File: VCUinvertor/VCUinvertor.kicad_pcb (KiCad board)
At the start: 2 copper layers, 154 x 113.8 mm, 71 parts, among them J1 NXP1, J2 Conn_02x10_Odd_Even, J3 NXP2, J4 Conn_02x10_Odd_Even, J5 Conn_02x10_Odd_Even, J6 Conn_02x10_Odd_Even, J7 PowerSupply, Q1 BSS138, Q10 BSS138, Q2 BSS138, Q3 BSS138, Q4 BSS138, Q5 BSS138, Q6 BSS138, Q7 BSS138, Q8 BSS138, Q9 BSS138, U1 TJA1448ATK, U2 REF3433T, U2 TJA1443ATK, U3 TLV76150DCY

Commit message: Footprint assignment
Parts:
- removed the U2 at (148.1, 100.9)
- added C1: 0.1uF, Capacitor_SMD:C_0805_2012Metric_Pad1.18x1.45mm_HandSolder, F.Cu at (204.1, 92.4)
- added C10: 0.1uF, Capacitor_SMD:C_0805_2012Metric_Pad1.18x1.45mm_HandSolder, F.Cu at (208.9, 101.5)
- added C11: 10uF, Capacitor_SMD:C_0805_2012Metric_Pad1.18x1.45mm_HandSolder, F.Cu at (208.9, 104.5)
- added C2: 0.1uF, Capacitor_SMD:C_0805_2012Metric_Pad1.18x1.45mm_HandSolder, F.Cu at (204.1, 95.4)
- added C3: 0.1uF, Capacitor_SMD:C_0805_2012Metric_Pad1.18x1.45mm_HandSolder, F.Cu at (204.1, 98.5)
- added C4: 2.2uF, Capacitor_SMD:C_0805_2012Metric_Pad1.18x1.45mm_HandSolder, F.Cu at (204.1, 101.5)
- added C5: 0.1uF, Capacitor_SMD:C_0805_2012Metric_Pad1.18x1.45mm_HandSolder, F.Cu at (204.1, 104.5)
- added C6: 0.1uF, Capacitor_SMD:C_0805_2012Metric_Pad1.18x1.45mm_HandSolder, F.Cu at (204.1, 107.5)
- added C7: 4.7uF, Capacitor_SMD:C_0805_2012Metric_Pad1.18x1.45mm_HandSolder, F.Cu at (208.9, 92.4)
- added C8: 4.7uF, Capacitor_SMD:C_0805_2012Metric_Pad1.18x1.45mm_HandSolder, F.Cu at (208.9, 95.4)
- added C9: 10uF, Capacitor_SMD:C_0805_2012Metric_Pad1.18x1.45mm_HandSolder, F.Cu at (208.9, 98.5)
- added DAC1: LTC2645HMS-L12_PBF, Package_SO:MSOP-16-1EP_3x4.039mm_P0.5mm_EP1.651x2.845mm, F.Cu at (164.1, 100.2)
- added Q1: BSS138, Package_TO_SOT_SMD:SOT-23, F.Cu at (194.3, 93.2)
- added Q10: BSS138, Package_TO_SOT_SMD:SOT-23, F.Cu at (199.2, 111.0)
- added Q2: BSS138, Package_TO_SOT_SMD:SOT-23, F.Cu at (194.3, 97.6)
- added Q3: BSS138, Package_TO_SOT_SMD:SOT-23, F.Cu at (194.3, 102.0)
- added Q4: BSS138, Package_TO_SOT_SMD:SOT-23, F.Cu at (194.3, 106.5)
- added Q5: BSS138, Package_TO_SOT_SMD:SOT-23, F.Cu at (194.3, 111.0)
- added Q6: BSS138, Package_TO_SOT_SMD:SOT-23, F.Cu at (199.2, 93.2)
- added Q7: BSS138, Package_TO_SOT_SMD:SOT-23, F.Cu at (199.2, 97.6)
- added Q8: BSS138, Package_TO_SOT_SMD:SOT-23, F.Cu at (199.2, 102.0)
- added Q9: BSS138, Package_TO_SOT_SMD:SOT-23, F.Cu at (199.2, 106.5)
- added R1: 60R4, Resistor_SMD:R_0805_2012Metric, F.Cu at (176.4, 92.4)
- added R10: 5k, Resistor_SMD:R_0805_2012Metric, F.Cu at (180.8, 95.3)
- added R11: 5k, Resistor_SMD:R_0805_2012Metric, F.Cu at (180.8, 98.3)
- added R12: 5k, Resistor_SMD:R_0805_2012Metric, F.Cu at (180.8, 101.2)
- added R13: 5k, Resistor_SMD:R_0805_2012Metric, F.Cu at (180.8, 104.2)
- added R14: 5k, Resistor_SMD:R_0805_2012Metric, F.Cu at (180.8, 107.2)
- added R15: 10k, Resistor_SMD:R_0805_2012Metric, F.Cu at (180.8, 110.1)
- added R16: 5k, Resistor_SMD:R_0805_2012Metric, F.Cu at (180.8, 113.0)
- added R17: 10k, Resistor_SMD:R_0805_2012Metric, F.Cu at (185.3, 92.4)
- added R18: 5k, Resistor_SMD:R_0805_2012Metric, F.Cu at (185.3, 95.3)
- added R19: 10k, Resistor_SMD:R_0805_2012Metric, F.Cu at (185.3, 98.3)
- added R2: 60R4, Resistor_SMD:R_0805_2012Metric, F.Cu at (176.4, 95.3)
- added R20: 5k, Resistor_SMD:R_0805_2012Metric, F.Cu at (185.3, 101.2)
- added R21: 10k, Resistor_SMD:R_0805_2012Metric, F.Cu at (185.3, 104.2)
- added R22: 5k, Resistor_SMD:R_0805_2012Metric, F.Cu at (185.3, 107.2)
- added R23: 10k, Resistor_SMD:R_0805_2012Metric, F.Cu at (185.3, 110.1)
- added R24: 5k, Resistor_SMD:R_0805_2012Metric, F.Cu at (185.3, 113.0)
- added R25: 5.1k, Resistor_SMD:R_0805_2012Metric, F.Cu at (189.7, 92.4)
- added R26: 10k, Resistor_SMD:R_0805_2012Metric, F.Cu at (189.7, 95.3)
- added R27: 5.1k, Resistor_SMD:R_0805_2012Metric, F.Cu at (189.7, 98.3)
- added R28: 10k, Resistor_SMD:R_0805_2012Metric, F.Cu at (189.7, 101.2)
- added R3: 60R4, Resistor_SMD:R_0805_2012Metric, F.Cu at (176.4, 98.3)
- added R4: 60R4, Resistor_SMD:R_0805_2012Metric, F.Cu at (176.4, 101.2)
- added R5: 10k, Resistor_SMD:R_0805_2012Metric, F.Cu at (176.4, 104.2)
- added R6: 10k, Resistor_SMD:R_0805_2012Metric, F.Cu at (176.4, 107.2)
- added R7: 10k, Resistor_SMD:R_0805_2012Metric, F.Cu at (176.4, 110.1)
- added R8: 10k, Resistor_SMD:R_0805_2012Metric, F.Cu at (176.4, 113.0)
- added R9: 10k, Resistor_SMD:R_0805_2012Metric, F.Cu at (180.8, 92.4)
- moved JO19 121.0 mm to (249.5, 130.5), turned to 90 degrees
- moved JO11 118.7 mm to (244.8, 130.5), turned to 90 degrees
- moved JO9 116.6 mm to (240.2, 130.5), turned to 90 degrees
- moved JO5 114.9 mm to (235.5, 130.5), turned to 90 degrees
- moved JO3 113.6 mm to (230.9, 130.5), turned to 90 degrees
- moved JO1 76.6 mm to (231.8, 93.6)
- moved JO13 76.6 mm to (246.3, 93.6)
- moved JO14 76.6 mm to (246.3, 98.2)
- moved JO15 76.6 mm to (246.3, 102.9)
- moved JO16 76.6 mm to (246.3, 107.5)
- moved JO17 76.6 mm to (251.2, 93.6)
- moved JO18 76.6 mm to (251.2, 98.2)
- moved JO19 76.6 mm to (251.2, 102.9)
- moved JO2 76.6 mm to (231.8, 98.2)
- moved JO20 76.6 mm to (251.2, 107.5)
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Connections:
- J3 pad 10: unconnected-(J3-Pin_10-Pad10) -> /TX1
- J3 pad 12: unconnected-(J3-Pin_12-Pad12) -> /RX1
- J3 pad 18: unconnected-(J3-Pin_18-Pad18) -> NXP_TPSOUT01
- J3 pad 2: unconnected-(J3-Pin_2-Pad2) -> /Pxx
- J3 pad 20: unconnected-(J3-Pin_20-Pad20) -> NXP_TPSOUT02
- J3 pad 4: unconnected-(J3-Pin_4-Pad4) -> /Pyy
- J3 pad 6: unconnected-(J3-Pin_6-Pad6) -> /TX0
- J3 pad 8: unconnected-(J3-Pin_8-Pad8) -> /RX0
- J4 pad 10: unconnected-(J4-Pin_10-Pad10) -> /NXP_ACC01
- J4 pad 12: unconnected-(J4-Pin_12-Pad12) -> /NXP_ECO01
- J4 pad 14: unconnected-(J4-Pin_14-Pad14) -> /NXP_BRK01
- J4 pad 16: unconnected-(J4-Pin_16-Pad16) -> /NXP_FWD01
- J4 pad 18: unconnected-(J4-Pin_18-Pad18) -> /NXP_REV01
- J4 pad 2: unconnected-(J4-Pin_2-Pad2) -> /PWM_NXP4
- J4 pad 20: unconnected-(J4-Pin_20-Pad20) -> BACKLIGHT_ON
- J4 pad 4: unconnected-(J4-Pin_4-Pad4) -> /PWM_NXP3
- J4 pad 6: unconnected-(J4-Pin_6-Pad6) -> /PWM_NXP2
- J4 pad 8: unconnected-(J4-Pin_8-Pad8) -> /PWM_NXP1
- J6 pad 10: unconnected-(J6-Pin_10-Pad10) -> /NXP_REV02
- J6 pad 2: unconnected-(J6-Pin_2-Pad2) -> /NXP_ACC02
- J6 pad 4: unconnected-(J6-Pin_4-Pad4) -> /NXP_ECO02
- J6 pad 6: unconnected-(J6-Pin_6-Pad6) -> /NXP_BRK02
- J6 pad 8: unconnected-(J6-Pin_8-Pad8) -> /NXP_FWD02
- JO11 pad 1: Net-(JO11-Pin_1) -> /ECO1
- JO19 pad 1: Net-(JO19-Pin_1) -> /ACC1
- JO22 pad 1: Net-(JO22-Pin_1) -> /REV2
- JO23 pad 1: Net-(JO23-Pin_1) -> /FWD2
- JO25 pad 1: Net-(JO25-Pin_1) -> /H_Brk2
- JO29 pad 1: Net-(JO29-Pin_1) -> /ECO2
- JO3 pad 1: Net-(JO3-Pin_1) -> /REV1
- JO31 pad 1: Net-(JO31-Pin_1) -> /ACC2
- JO5 pad 1: Net-(JO5-Pin_1) -> /FWD1
- JO9 pad 1: Net-(JO9-Pin_1) -> /H_Brk1
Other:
- board size 154 x 113.8 mm -> 210.5 x 113.8 mm

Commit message: Layout_Global arrangement
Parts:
- removed D2: 1N4148WT, Diode_SMD:D_SOD-523
- removed the JO11 at (241.4, 102.9)
- removed JO16, JO17, JO18, JO20, JO36, JO37, JO38, JO39, JO40: -, Connector_Wire:SolderWire-0.75sqmm_1x01_D1.25mm_OD2.3mm
- removed the JO19 at (251.2, 102.9)
- removed JO2: -REV (Orange), Connector_Wire:SolderWire-0.75sqmm_1x01_D1.25mm_OD2.3mm
- removed the JO3 at (231.8, 102.9)
- removed the JO5 at (236.6, 93.6)
- removed the JO9 at (241.4, 93.6)
- removed the Q1 at (142.5, 65.5)
- removed the Q1 at (194.3, 93.2)
- removed the Q10 at (199.2, 111.0)
- removed the Q10 at (147.4, 83.3)
- removed the Q2 at (142.5, 70.0)
- removed the Q2 at (194.3, 97.6)
- removed the Q3 at (142.5, 74.4)
- removed the Q3 at (194.3, 102.0)
- removed the Q4 at (142.5, 78.9)
- removed the Q4 at (194.3, 106.5)
- removed the Q5 at (142.5, 83.3)
- removed the Q5 at (194.3, 111.0)
- removed the Q6 at (199.2, 93.2)
- removed the Q6 at (147.4, 65.5)
- removed the Q7 at (147.4, 70.0)
- removed the Q7 at (199.2, 97.6)
- removed the Q8 at (147.4, 74.4)
- removed the Q8 at (199.2, 102.0)
- removed the Q9 at (199.2, 106.5)
- removed the Q9 at (147.4, 78.9)
- added J8: CAN_NXP, Connector_PinHeader_2.54mm:PinHeader_1x04_P2.54mm_Vertical, B.Cu at (85.3, 48.0)
- added J9: BACKLIGHT, Connector_JST:JST_PH_B3B-PH-K_1x03_P2.00mm_Vertical, B.Cu at (110.0, 40.6)
- added Q1: BSS138, Package_TO_SOT_SMD:SOT-23, B.Cu at (126.3, 131.0)
- added Q10: BSS138, Package_TO_SOT_SMD:SOT-23, B.Cu at (126.0, 57.6)
- added Q2: BSS138, Package_TO_SOT_SMD:SOT-23, B.Cu at (126.3, 125.7)
- added Q3: BSS138, Package_TO_SOT_SMD:SOT-23, B.Cu at (126.3, 120.2)
- added Q4: BSS138, Package_TO_SOT_SMD:SOT-23, B.Cu at (126.8, 114.9)
- added Q5: BSS138, Package_TO_SOT_SMD:SOT-23, B.Cu at (127.1, 109.5)
- added Q6: BSS138, Package_TO_SOT_SMD:SOT-23, B.Cu at (125.4, 81.1)
- added Q7: BSS138, Package_TO_SOT_SMD:SOT-23, B.Cu at (125.5, 74.5)
- added Q8: BSS138, Package_TO_SOT_SMD:SOT-23, B.Cu at (125.8, 69.1)
- added Q9: BSS138, Package_TO_SOT_SMD:SOT-23, B.Cu at (125.8, 63.5)
- C3, C4, CA1, J7, JU1, JU2, R10, R11, R12, R13, R14, R15, R16, R17, R18, R19, R20, R21, R22, R23, R24, R5, R6, R7, R8, R9, U3: moved to B.Cu
- J1: value NXP1 -> NXP12
- J2: value Conn_02x10_Odd_Even -> NXP11
- J3: value NXP2 -> NXP15
- J4: value Conn_02x10_Odd_Even -> NXP14
- J5: value Conn_02x10_Odd_Even -> NXP10
- J6: value Conn_02x10_Odd_Even -> NXP13
- moved JU2 148.8 mm to (82.7, 146.9), turned to 180 degrees
- moved C10 134.5 mm to (75.2, 115.6), turned to 90 degrees
- moved C9 132.8 mm to (77.3, 115.6), turned to 90 degrees
- moved JU1 130.9 mm to (95.2, 146.8), turned to 180 degrees
- moved C4 123.1 mm to (88.0, 60.5), turned to 90 degrees
- moved C8 120.8 mm to (91.1, 121.8), turned to 180 degrees
- moved C7 120.4 mm to (91.2, 117.7), turned to 180 degrees
- moved C3 114.4 mm to (97.7, 56.4), turned to -90 degrees
- moved C11 112.6 mm to (97.3, 89.8), turned to -90 degrees
- moved JO14 110.9 mm to (141.4, 134.1), turned to 90 degrees
- moved C1 109.5 mm to (94.8, 98.2), turned to 90 degrees
- moved JO19 109.1 mm to (141.2, 116.8)
- moved JO34 107.7 mm to (141.4, 84.4)
- moved JO35 105.3 mm to (141.4, 67.6)
- moved C6 105.3 mm to (98.8, 108.5)
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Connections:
- net Net-(DAC1-VOUTA) renamed /Brk_AN1
- net Net-(DAC1-VOUTC) renamed /Brk_AN2
- J6 pad 13: unconnected-(J6-Pin_13-Pad13) -> GND
- J6 pad 15: unconnected-(J6-Pin_15-Pad15) -> +12V
- JO26 pad 1: GND -> unconnected-(JO26-Pin_1-Pad1)
- JO6 pad 1: GND -> unconnected-(JO6-Pin_1-Pad1)
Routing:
- net GND: track 0.00 -> 24.6 mm
- net +5V: track 0.00 -> 17.1 mm
- net /Brk_AN2: track 0.00 -> 14.0 mm, vias 0 -> 1
- net +3.3V: track 0.00 -> 13.1 mm
- net /PWM_NXP3: track 0.00 -> 11.5 mm, vias 0 -> 1
- net /PWM_NXP4: track 0.00 -> 11.0 mm, vias 0 -> 1
- net /PWM_NXP1: track 0.00 -> 10.7 mm, vias 0 -> 1
- net /PWM_NXP2: track 0.00 -> 9.41 mm, vias 0 -> 1
- net /Brk_AN1: track 0.00 -> 7.60 mm, vias 0 -> 1
- net /H_Brk2: track 0.00 -> 6.94 mm
- net /REV2: track 0.00 -> 6.72 mm
- net /ECO2: track 0.00 -> 6.64 mm
- net unconnected-(JO26-Pin_1-Pad1): track 0.00 -> 6.44 mm
- net /CANL02: track 0.00 -> 6.00 mm
- net /CANH02: track 0.00 -> 5.40 mm
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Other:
- board size 210.5 x 113.8 mm -> 97.3 x 113.8 mm

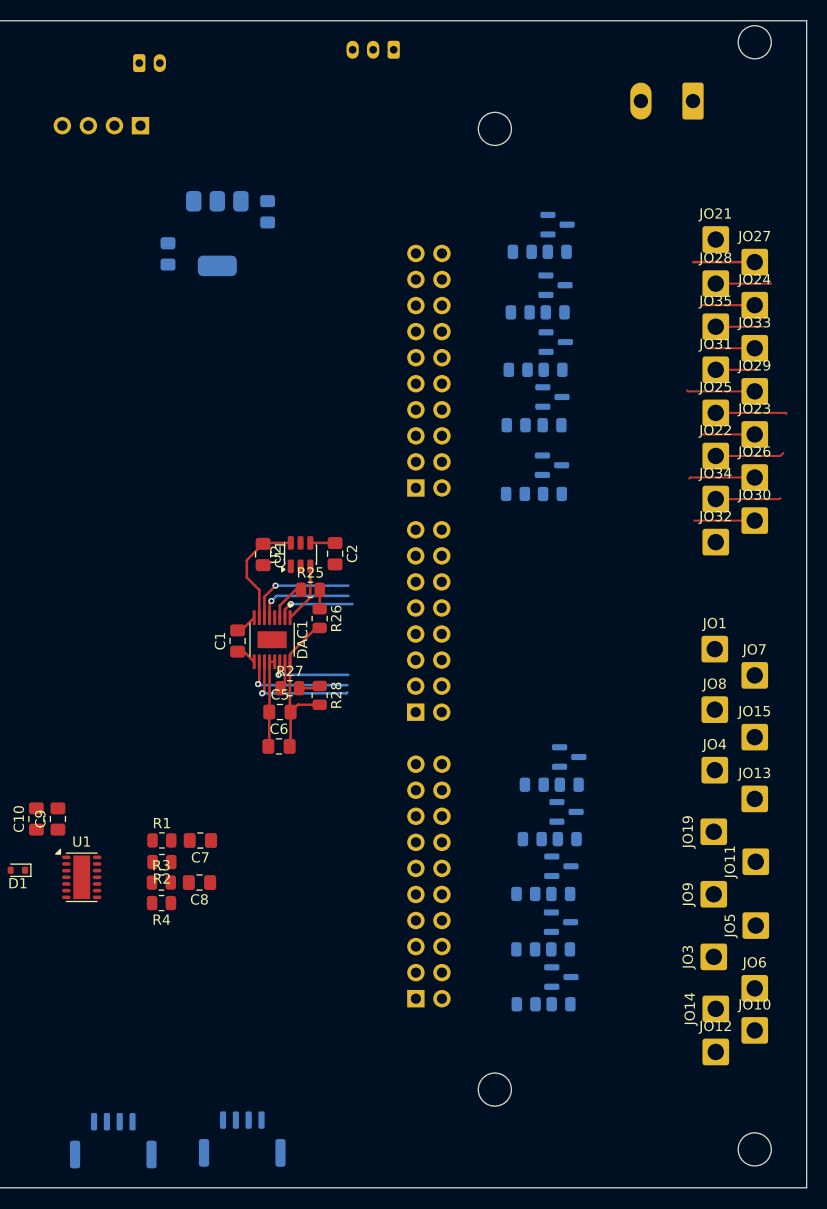
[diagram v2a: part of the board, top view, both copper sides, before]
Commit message: DAQ footprint correction
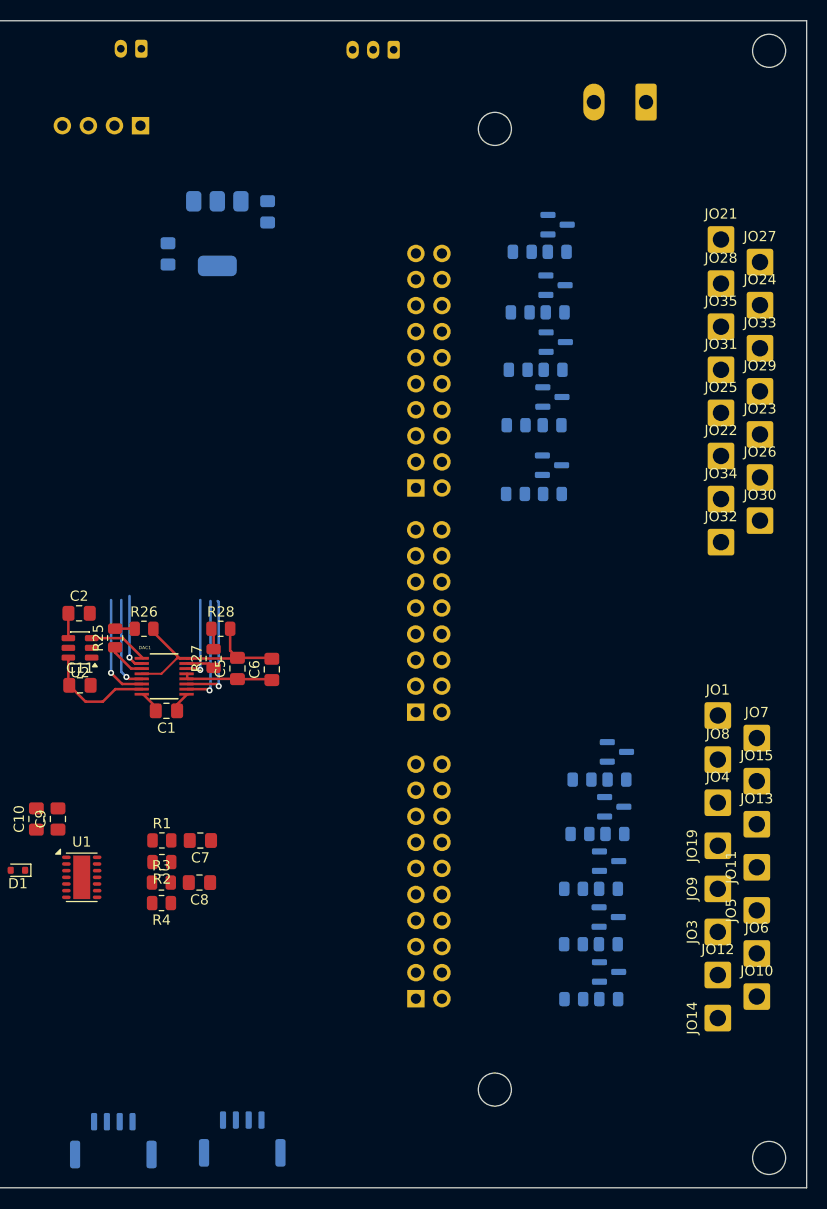
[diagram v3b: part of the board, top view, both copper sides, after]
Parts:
- DAC1: footprint Package_SO:MSOP-16-1EP_3x4.039mm_P0.5mm_EP1.651x2.845mm -> LTC2645HMS-L12_PBF:MSOP-16_MS
- moved C2 25.6 mm to (79.3, 95.5), turned to 0 degrees
- moved U2 23.3 mm to (79.4, 98.9), turned to 180 degrees
- moved C11 21.9 mm to (79.4, 102.6), turned to 0 degrees
- moved R25 19.6 mm to (82.8, 97.9), turned to 90 degrees
- moved R26 17.2 mm to (85.7, 97.0), turned to 0 degrees
- moved R28 11.6 mm to (93.1, 97.0), turned to 0 degrees
- moved DAC1 11.1 mm to (87.6, 101.7), turned to 0 degrees
- moved C1 9.72 mm to (87.8, 105.0), turned to 180 degrees
- moved R27 7.98 mm to (92.4, 99.9), turned to 90 degrees
- moved C6 7.54 mm to (98.1, 101.0), turned to 90 degrees
- moved JO12 7.50 mm to (141.6, 130.8)
- moved JO1 6.48 mm to (141.6, 105.5)
- moved JO7 6.11 mm to (145.4, 107.7)
- moved C5 5.93 mm to (94.8, 100.9), turned to 90 degrees
- moved JO8 4.88 mm to (141.6, 109.8)
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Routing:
- net /H_Brk2: track 6.94 -> 0.00 mm
- net /REV2: track 6.72 -> 0.00 mm
- net /ECO2: track 6.64 -> 0.00 mm
- net unconnected-(JO26-Pin_1-Pad1): track 6.44 -> 0.00 mm
- net /CANL02: track 6.00 -> 0.00 mm
- net /Brk_AN2: track 14.0 -> 8.13 mm
- net /CANH02: track 5.40 -> 0.00 mm
- net unconnected-(JO24-Pin_1-Pad1): track 5.10 -> 0.00 mm
- net /FWD2: track 5.10 -> 0.00 mm
- net unconnected-(JO35-Pin_1-Pad1): track 4.50 -> 0.00 mm
- net unconnected-(JO33-Pin_1-Pad1): track 4.50 -> 0.00 mm
- net /ACC2: track 4.10 -> 0.00 mm
- net GND: track 24.6 -> 23.3 mm
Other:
- outline, holes or cut-outs redrawn
